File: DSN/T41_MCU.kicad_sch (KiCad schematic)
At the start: 17 parts

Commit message: Added Footprints
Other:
- title: (none) -> Teensy 4.1 MCU
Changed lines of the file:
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@@
 (kicad_sch (version 20211123) (generator eeschema)
   (paper "A3")
+  (title_block
+    (title "Teensy 4.1 MCU")
+    (date "2023-03-07")
+    (rev "A")
+    (comment 1 "Designed by DragonEnjoyer :3")
+  )
   (junction (at 179.07 119.38) (diameter 0) (color 0 0 0 0)
   )

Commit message: Added component ref des
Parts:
- gave numbers to parts that had none: 17
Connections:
- net FPGA_1_IO8 is gone; now on net MCU_FPGA_1_IO8: U3.16 (24_A10_TX6_SCL2)
- net FPGA_1_IO9 is gone; now on net MCU_FPGA_1_IO9: U3.17 (25_A11_RX6_SDA2)
- net MUC_SPI1_SCLK renamed MCU_SPI1_SCLK
- no-connect marks 14 -> 15

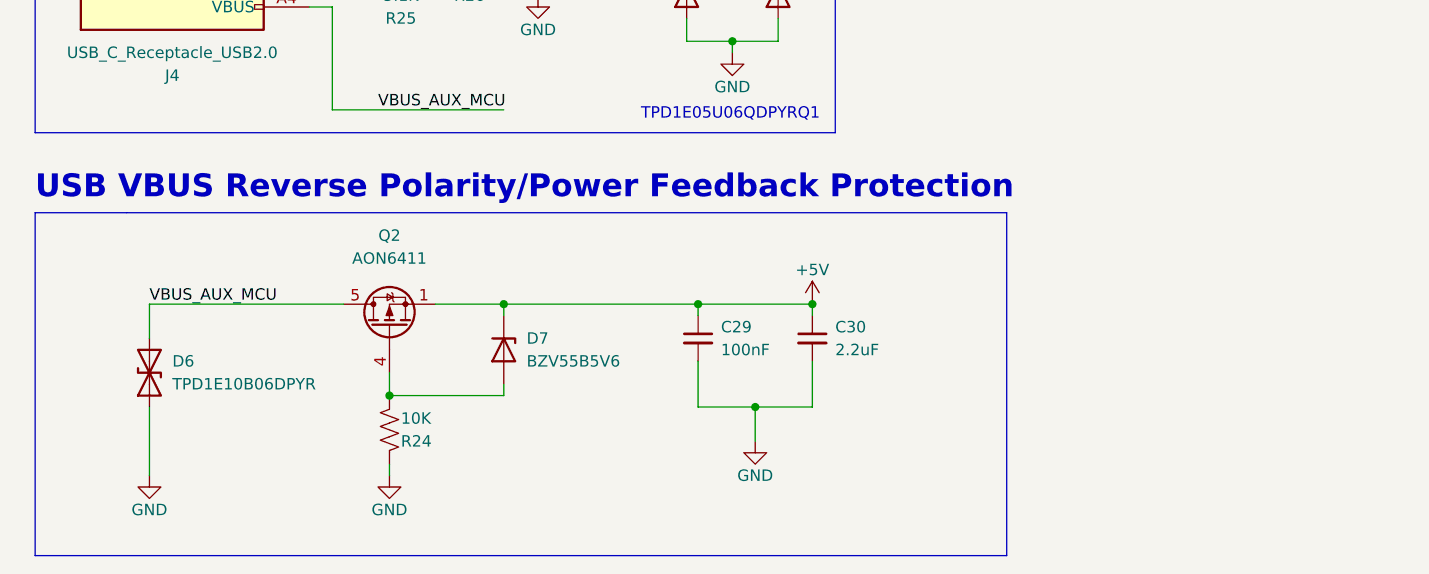
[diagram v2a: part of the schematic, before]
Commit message: Fixed all ERC Errors
Warnings can be ignored
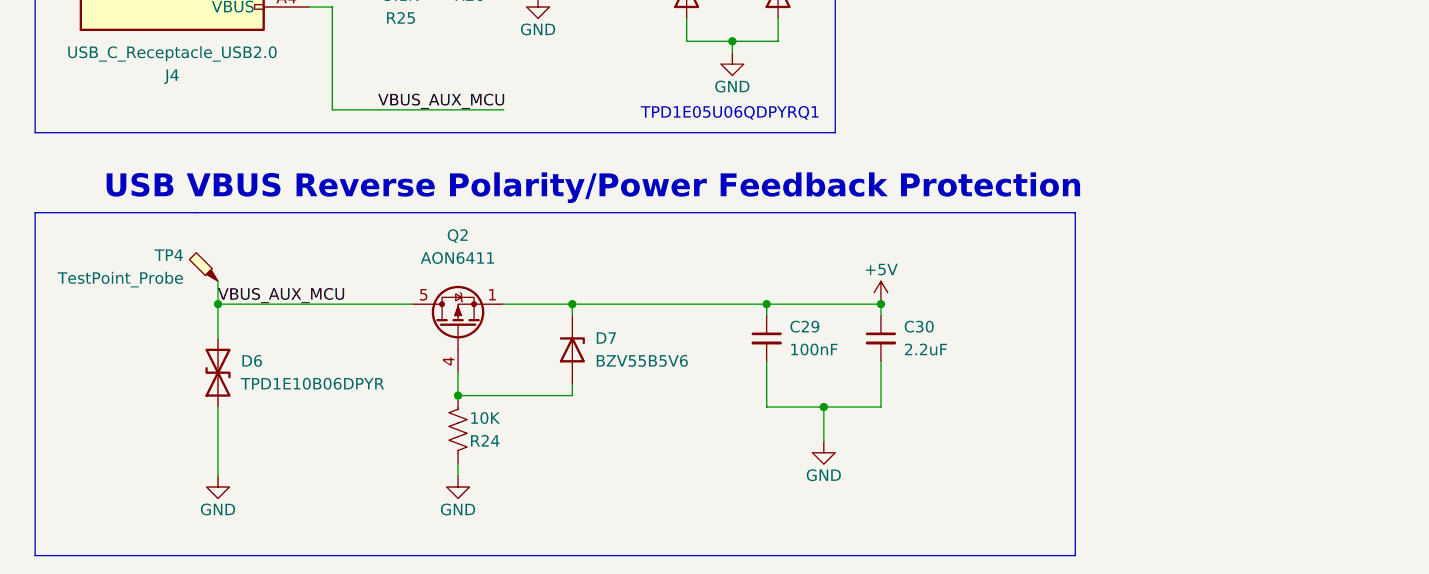
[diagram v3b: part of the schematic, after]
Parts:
- added TP4: TestPoint_Probe, TestPoint:TestPoint_Loop_D2.50mm_Drill1.85mm, symbol Connector:TestPoint_Probe
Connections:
- net VBUS_AUX_MCU: now also TP4.1
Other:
- moved on the sheet: C29, C30, D6, D7, Q2, R24
